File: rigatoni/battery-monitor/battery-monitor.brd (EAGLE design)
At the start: 160 x 100 mm, 35 parts, among them J1 S2B-XH-A_(LF)(SN), J2 XF2C-2555-41A, J4 S4B-XH-A(LF)(SN), U1 LT1930ES5TRMPBF_BOOST_CONV, U2 ETH-POE, U3 STM32H743ZIT6

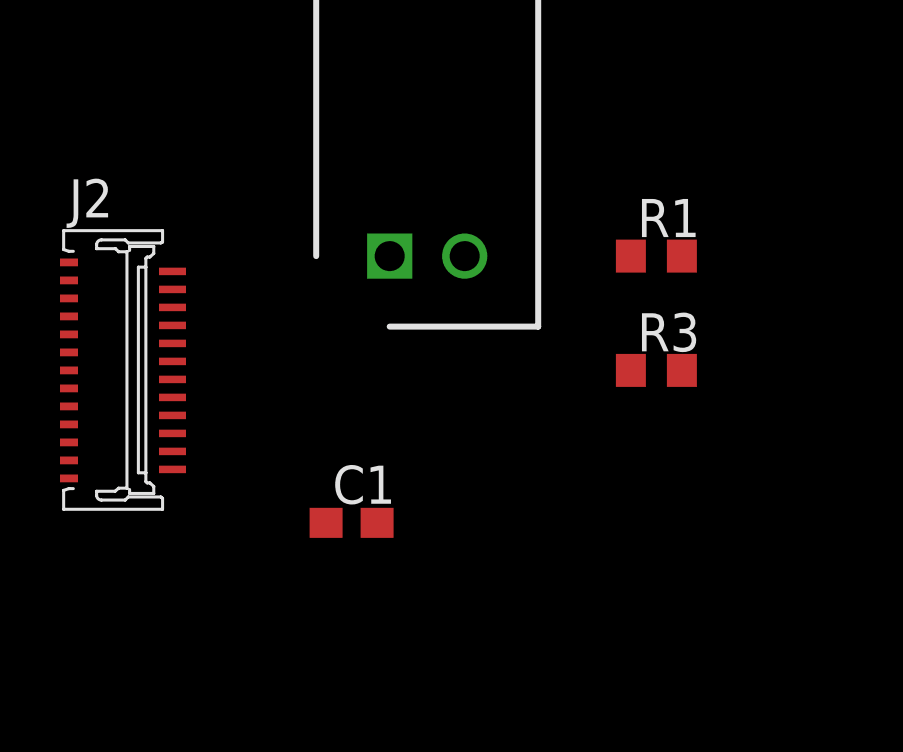
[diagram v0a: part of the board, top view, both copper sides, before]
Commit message: Fix R1 value
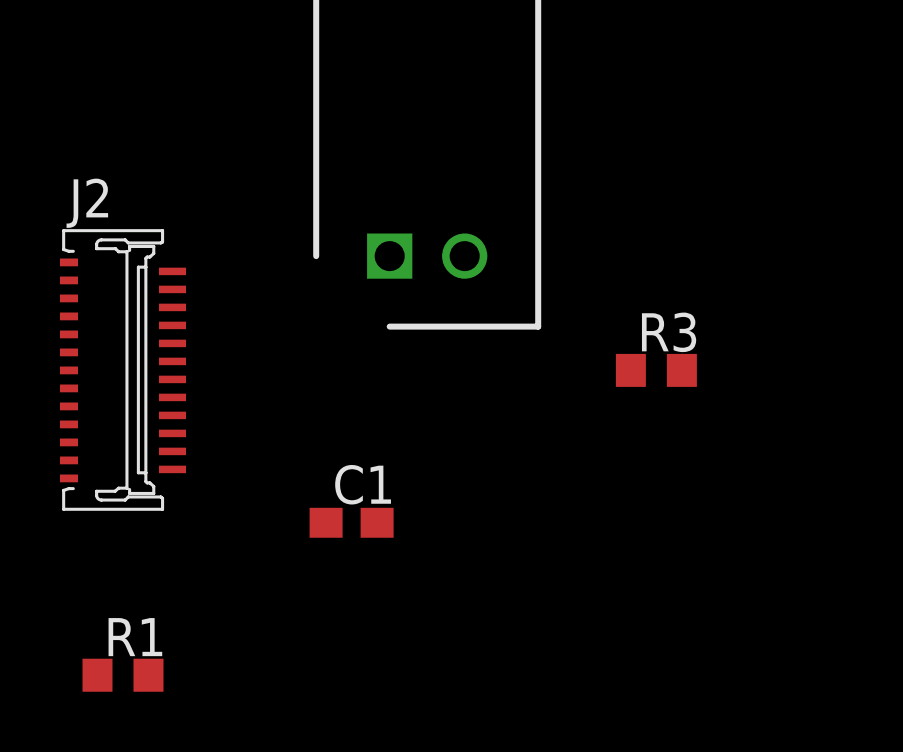
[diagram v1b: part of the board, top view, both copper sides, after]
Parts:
- moved R1 22.6 mm to (-91.4, -16.5)
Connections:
- net GND: now also R1.2; no longer R1.1
- net VOLT_DATA: now also R1.1; no longer R1.2
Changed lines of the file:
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@@
 <attribute name="VALUE" x="-34.7472" y="56.515" size="1.27" layer="27" ratio="6" rot="SR0"/>
-</element>
-<element name="R1" library="rcl" library_urn="urn:adsk.eagle:library:334" package="R0603" package3d_urn="urn:adsk.eagle:package:23555/3" value="5 kΩ" x="-73.66" y="-2.54" smashed="yes">
-<attribute name="NAME" x="-74.295" y="-1.905" size="1.27" layer="25"/>
-<attribute name="POPULARITY" value="77" x="-73.66" y="-2.54" size="1.778" layer="27" display="off"/>
-<attribute name="SPICEPREFIX" value="R" x="-73.66" y="-2.54" size="1.778" layer="27" display="off"/>
-<attribute name="VALUE" x="-74.295" y="-4.445" size="1.27" layer="27"/>
 </element>
 <element name="R3" library="rcl" library_urn="urn:adsk.eagle:library:334" package="R0603" package3d_urn="urn:adsk.eagle:package:23555/3" value="55 kΩ" x="-73.66" y="-6.35" smashed="yes">
@@
 <attribute name="OC_NEWARK" value="78M3584" x="-91.44" y="-6.35" size="1.778" layer="27" display="off"/>
 <attribute name="VALUE" x="-93.24" y="-12.65" size="1.27" layer="27"/>
+</element>
+<element name="R1" library="rcl" library_urn="urn:adsk.eagle:library:334" package="R0603" package3d_urn="urn:adsk.eagle:package:23555/3" value="5 kΩ" x="-91.44" y="-16.51" smashed="yes">
+<attribute name="NAME" x="-92.075" y="-15.875" size="1.27" layer="25"/>
+<attribute name="POPULARITY" value="77" x="-91.44" y="-16.51" size="1.778" layer="27" display="off"/>
+<attribute name="SPICEPREFIX" value="R" x="-91.44" y="-16.51" size="1.778" layer="27" display="off"/>
+<attribute name="VALUE" x="-92.075" y="-18.415" size="1.27" layer="27"/>
 </element>
 </elements>
@@
 <contactref element="R2" pad="1"/>
 <contactref element="LD5" pad="A"/>
-<contactref element="R1" pad="1"/>
 <contactref element="J1" pad="2"/>
 <contactref element="C1" pad="2"/>
+<contactref element="R1" pad="2"/>
+<wire x1="-82.97" y1="-11.43" x2="-90.59" y2="-16.51" width="0" layer="19" extent="1-1"/>
 <wire x1="-80.05" y1="-2.54" x2="-82.97" y2="-11.43" width="0" layer="19" extent="1-1"/>
-<wire x1="-74.51" y1="-2.54" x2="-80.05" y2="-2.54" width="0" layer="19" extent="1-1"/>
-<wire x1="-55.15" y1="10.38" x2="-74.51" y2="-2.54" width="0" layer="19" extent="1-1"/>
+<wire x1="-55.15" y1="10.38" x2="-80.05" y2="-2.54" width="0" layer="19" extent="1-1"/>
 <wire x1="-65.91" y1="58.42" x2="-55.15" y2="10.38" width="0" layer="19" extent="1-1"/>
 <wire x1="-75.06" y1="58.42" x2="-65.91" y2="58.42" width="0" layer="19" extent="1-1"/>
@@
 <signal name="VOLT_DATA">
 <contactref element="R3" pad="2"/>
-<contactref element="R1" pad="2"/>
 <contactref element="U3" pad="35"/>
 <contactref element="C1" pad="1"/>
+<contactref element="R1" pad="1"/>
+<wire x1="-84.67" y1="-11.43" x2="-92.29" y2="-16.51" width="0" layer="19" extent="1-1"/>
 <wire x1="-72.81" y1="-6.35" x2="-84.67" y2="-11.43" width="0" layer="19" extent="1-1"/>
-<wire x1="-72.81" y1="-2.54" x2="-72.81" y2="-6.35" width="0" layer="19" extent="1-1"/>
-<wire x1="-36.025" y1="61.6" x2="-72.81" y2="-2.54" width="0" layer="19" extent="1-1"/>
+<wire x1="-36.025" y1="61.6" x2="-72.81" y2="-6.35" width="0" layer="19" extent="1-1"/>
 </signal>
 <signal name="N$1">

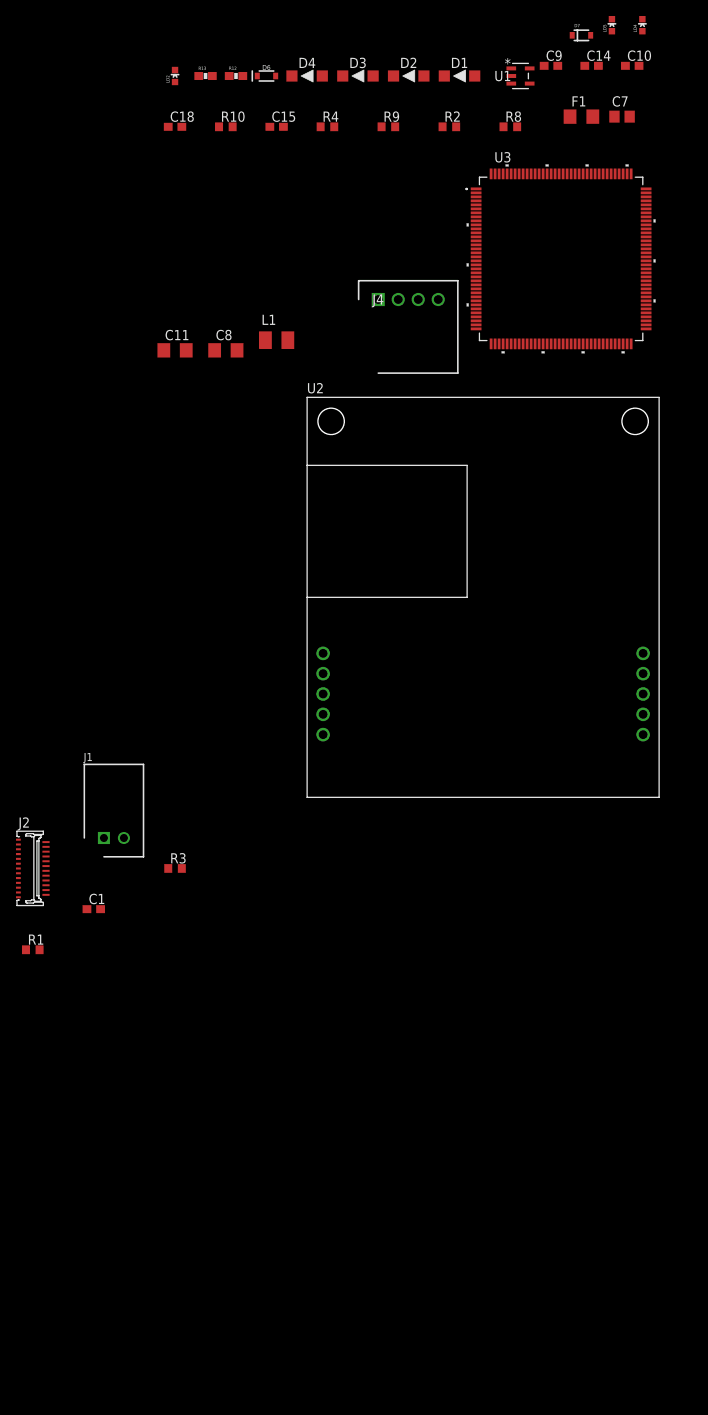
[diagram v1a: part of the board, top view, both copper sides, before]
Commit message: Removed Ethernet Header and MCU from schematic
Also updated RoboRacing_STM library
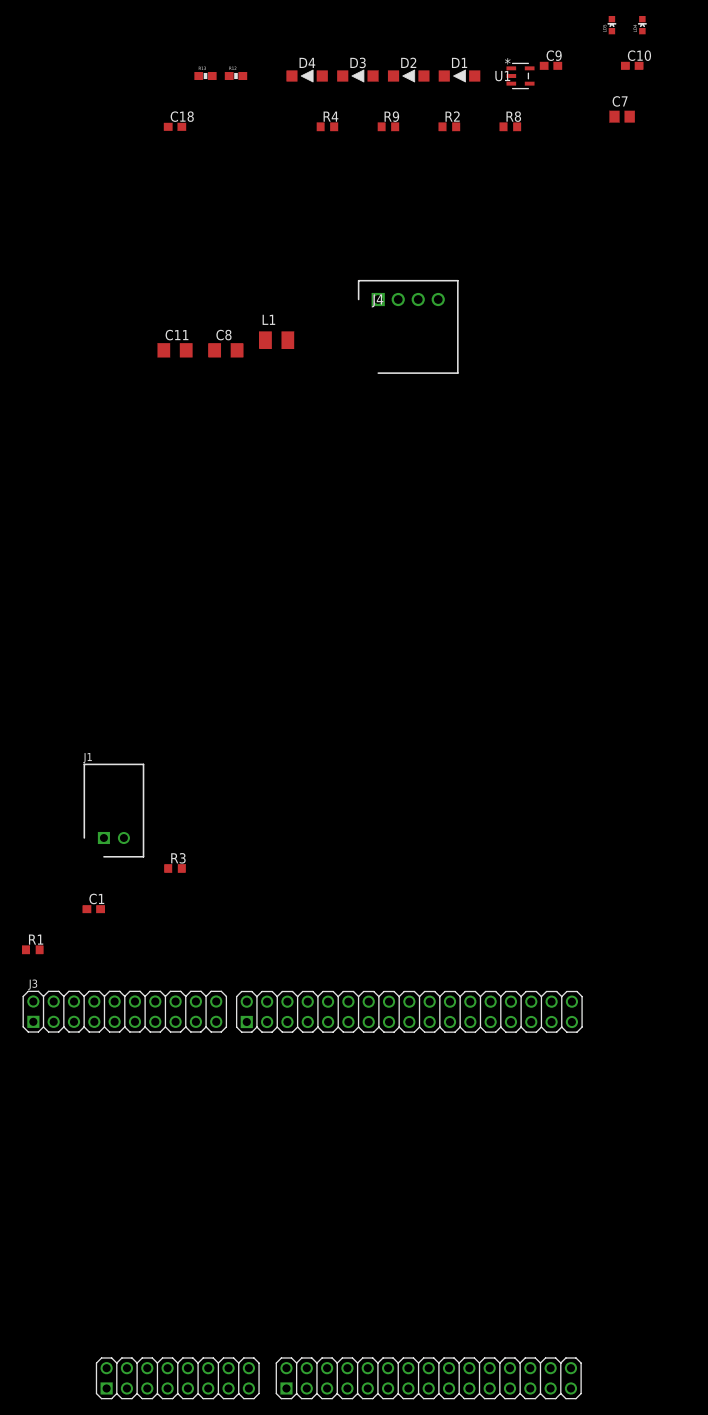
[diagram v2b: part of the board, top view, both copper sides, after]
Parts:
- removed C14: 1uF, rcl:C0603
- removed C15: 0.1uF, rcl:C0603
- removed D6: 5.1V, SparkFun-DiscreteSemi:SOD-323
- removed D7: (no value), RoboJackets-Diodes:SOD-323
- removed F1: 0.3A, RoboJackets-Passive:F1206
- removed J2: XF2C-2555-41A, con-omron:XF2C-2555-41A
- removed LD2: GREEN, SparkFun:LED-0603
- removed R10: 10kΩ, rcl:R0603
- removed U2: ETH-POE, ethernet_poe:HDRVR10W64P4000X254_2X5_1016X508X254B
- removed U3: STM32H743ZIT6, RoboRacing_STM:LQFP144-20X20MM
- added J3: STM32H743ZIT6_HEADER, RoboRacing_STM:2X08_2X15_2X10_2X17
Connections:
- removed net ETH_RST: U2.2
- removed net INT_ETH: U2.10
- removed net MISO: U2.8
- removed net MOSI: U2.9
- removed net N$10: D7.A, F1.1
- removed net N$4: F1.2, U2.3
- removed net SCLK: U2.7
- removed net SCNN: R10.1, U2.6
- removed net VBAT: U3.6
- removed net VCAP1: U3.71
- removed net VCAP2: U3.106
- removed net VDD: U3.144
- removed net VDD33USB: U3.95
- removed net VDDA: U3.33
- removed net VDD_10: U3.121
- removed net VDD_11: U3.131
- removed net VDD_2: U3.17
- removed net VDD_3: U3.30
- removed net VDD_4: U3.39
- removed net VDD_5: U3.52
- removed net VDD_6: U3.62
- removed net VDD_7: U3.72
- removed net VDD_8: U3.84
- removed net VDD_9: U3.108
- removed net VREF+: U3.32
- removed net VSS: U3.130
- removed net VSSA: U3.31
- removed net VSS_2: U3.16
- removed net VSS_3: U3.38
- removed net VSS_4: U3.51
- removed net VSS_5: U3.61
- removed net VSS_6: U3.83
- removed net VSS_7: U3.94
- removed net VSS_8: U3.107
- removed net VSS_9: U3.120
- net +5V: no longer C14.1, C15.1, D6.C, D7.C, LD2.A, R10.2
- net CURR_DATA: now also J3.17; no longer U3.36
- net GND: no longer C14.2, C15.2, D6.A, LD2.C, U2.5
- net VOLT_DATA: now also J3.19; no longer U3.35

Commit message: Updated Schematic with new Nucleo Header
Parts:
- removed J3: STM32H743ZIT6_HEADER, RoboRacing_STM:2X08_2X15_2X10_2X17
- added U2: NUCLEO-H743ZI-HEADER, RoboRacing_STM:MODULE_NUCLEO-HEADER
- moved J1 162.4 mm to (80.0, -17.8)
- moved C1 149.9 mm to (66.0, -16.5), turned to 270 degrees
- moved R1 149.9 mm to (58.4, -16.5), turned to 270 degrees
- moved R3 140.4 mm to (66.0, -20.7), turned to 90 degrees
- moved C7 26.9 mm to (8.89, 91.4)
- moved C11 19.9 mm to (-55.9, 49.5)
- moved LD5 18.3 mm to (-3.81, 88.9)
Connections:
- new net +3V3: U2.CN11_16
- new net +3V3_CN8: U2.CN8_7
- new net +5V_CN8: U2.CN8_9
- new net AGND_CN10: U2.CN10_3
- new net AGND_CN12: U2.CN12_32
- new net AREF: U2.CN7_6
- new net AVDD_CN10: U2.CN10_1
- new net AVDD_CN12: U2.CN12_7
- new net E5V: U2.CN11_6
- new net GND_CN10: U2.CN10_17, U2.CN10_22, U2.CN10_27, U2.CN10_5
- new net GND_CN11: U2.CN11_19, U2.CN11_20, U2.CN11_22, U2.CN11_49, U2.CN11_60, U2.CN11_71, U2.CN11_72, U2.CN11_8
- new net GND_CN12: U2.CN12_20, U2.CN12_39, U2.CN12_54, U2.CN12_63, U2.CN12_71, U2.CN12_72, U2.CN12_9
- new net GND_CN7: U2.CN7_8
- new net GND_CN8: U2.CN8_11, U2.CN8_13
- new net GND_CN9: U2.CN9_12, U2.CN9_23
- new net U5V: U2.CN12_8
- new net VBAT: U2.CN11_33
- new net VDD: U2.CN11_5
- new net VIN: U2.CN11_24
- new net VIN_CN8: U2.CN8_15
- net +5V: now also U2.CN11_18
- net CURR_DATA: now also U2.CN9_1; no longer J3.17
- net VOLT_DATA: now also U2.CN9_3; no longer J3.19
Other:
- board size 160 x 100 mm -> 69.8 x 133.3 mm
